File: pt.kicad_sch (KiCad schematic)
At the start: 7 parts, among them J6 PT

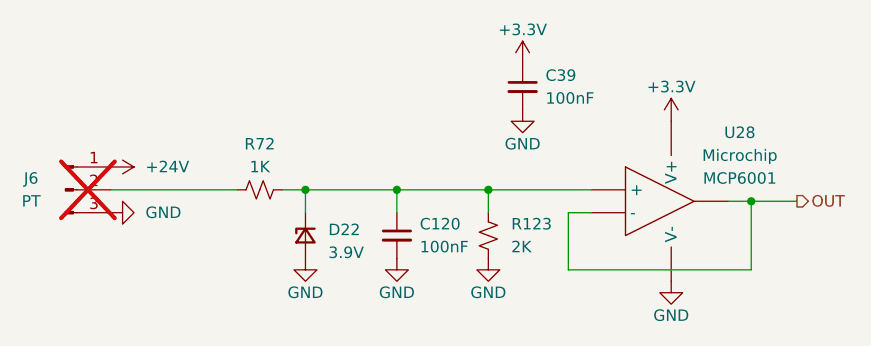
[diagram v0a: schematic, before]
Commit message: changed charging circuit for Insta360, gonna send in now on JLCPCB
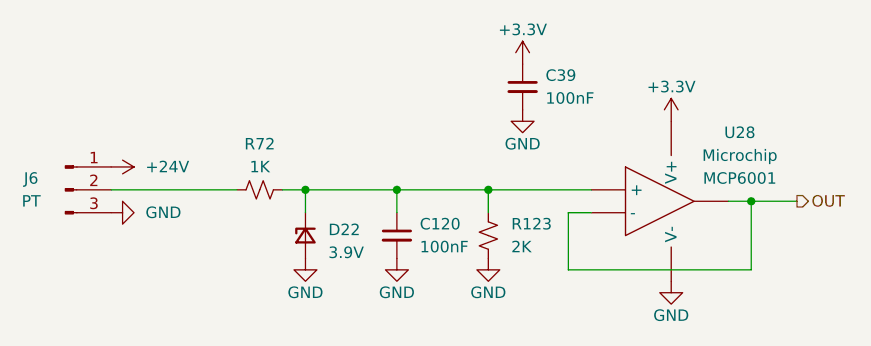
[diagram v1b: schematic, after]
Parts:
- J6: now fitted
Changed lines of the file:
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@@
 			)
 		)
-		(property "Description" ""
+		(property "Description" "Power symbol creates a global label with name \"+24V\""
 			(at 33.02 83.82 0)
 			(effects
@@
 		(in_bom yes)
 		(on_board yes)
-		(dnp yes)
+		(dnp no)
 		(property "Reference" "J6"
 			(at 24.13 85.09 0)
@@
 			)
 		)
-		(property "Description" ""
+		(property "Description" "Generic connector, single row, 01x03, script generated"
 			(at 27.94 86.36 0)
 			(effects
@@
 			)
 		)
-		(property "Description" ""
+		(property "Description" "Resistor, small US symbol"
 			(at 49.53 86.36 0)
 			(effects
@@
 			)
 		)
-		(property "Description" ""
+		(property "Description" "Resistor, small US symbol"
 			(at 74.93 91.44 0)
 			(effects
@@
 			)
 		)
-		(property "Description" ""
+		(property "Description" "Power symbol creates a global label with name \"GND\" , ground"
 			(at 64.77 93.98 0)
 			(effects
@@
 			)
 		)
-		(property "Description" ""
+		(property "Description" "Power symbol creates a global label with name \"GND\" , ground"
 			(at 74.93 93.98 0)
 			(effects
@@
 			)
 		)
-		(property "Description" ""
+		(property "Description" "Power symbol creates a global label with name \"GND\" , ground"
 			(at 54.61 93.98 0)
 			(effects
@@
 			)
 		)
-		(property "Description" ""
+		(property "Description" "Power symbol creates a global label with name \"GND\" , ground"
 			(at 33.02 88.9 0)
 			(effects
@@
 			)
 		)
-		(property "Description" ""
+		(property "Description" "Power symbol creates a global label with name \"+3.3V\""
 			(at 78.74 72.39 0)
 			(effects
@@
 			)
 		)
-		(property "Description" ""
+		(property "Description" "Power symbol creates a global label with name \"+3.3V\""
 			(at 95.25 78.74 0)
 			(effects
@@
 			)
 		)
-		(property "Description" ""
+		(property "Description" "Unpolarized capacitor, small symbol"
 			(at 78.74 74.93 0)
 			(effects
@@
 			)
 		)
-		(property "Description" ""
+		(property "Description" "Power symbol creates a global label with name \"GND\" , ground"
 			(at 78.74 77.47 0)
 			(effects
@@
 			)
 		)
-		(property "Description" ""
+		(property "Description" "Power symbol creates a global label with name \"GND\" , ground"
 			(at 95.25 96.52 0)
 			(effects
@@
 			)
 		)
-		(property "Description" ""
+		(property "Description" "Unpolarized capacitor, small symbol"
 			(at 64.77 91.44 0)
 			(effects

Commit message: fixing docs sruture
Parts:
- J6: footprint 0UCIRP-KiCAD-Lib:GX-12 3 pin -> UCIRP-KiCAD-Lib:GX-12 3 pin
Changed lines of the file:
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@@
 			)
 		)
-		(property "Footprint" "0UCIRP-KiCAD-Lib:GX-12 3 pin"
+		(property "Footprint" "UCIRP-KiCAD-Lib:GX-12 3 pin"
 			(at 27.94 86.36 0)
 			(effects
